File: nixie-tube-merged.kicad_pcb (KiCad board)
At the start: 2 copper layers, 99.8 x 97.5 mm, 0 parts

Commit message: finalized everything and ready to send out
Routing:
- net (no net): track 5710.5 -> 0.00 mm, vias 964 -> 0

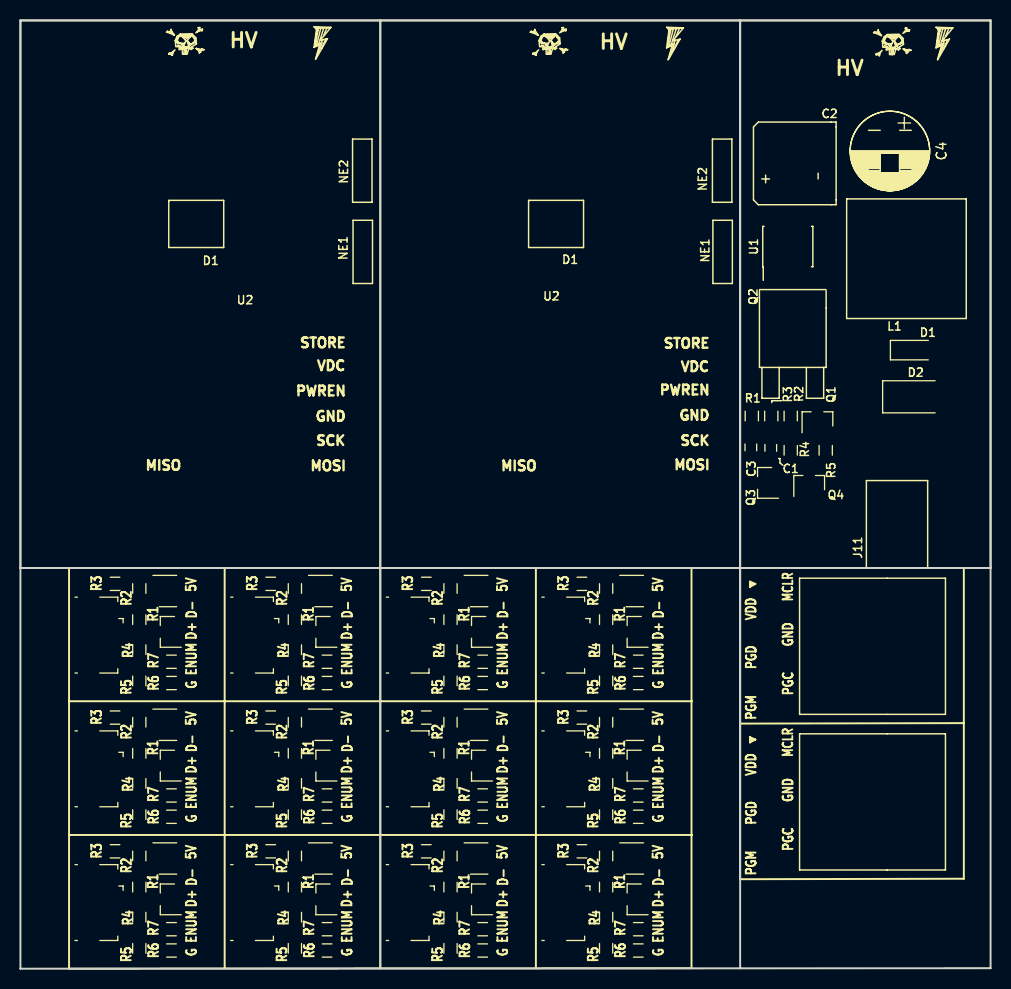
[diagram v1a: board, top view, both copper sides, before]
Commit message: added via stiching around the board
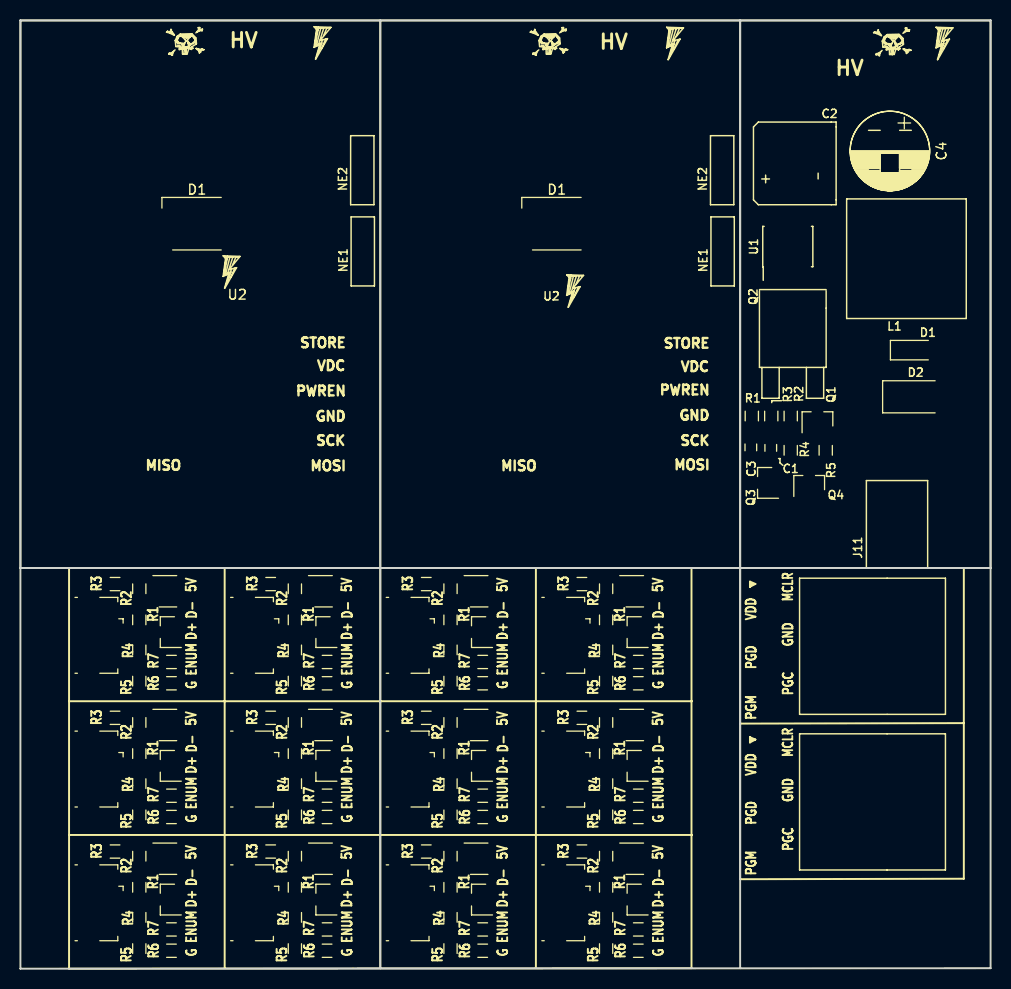
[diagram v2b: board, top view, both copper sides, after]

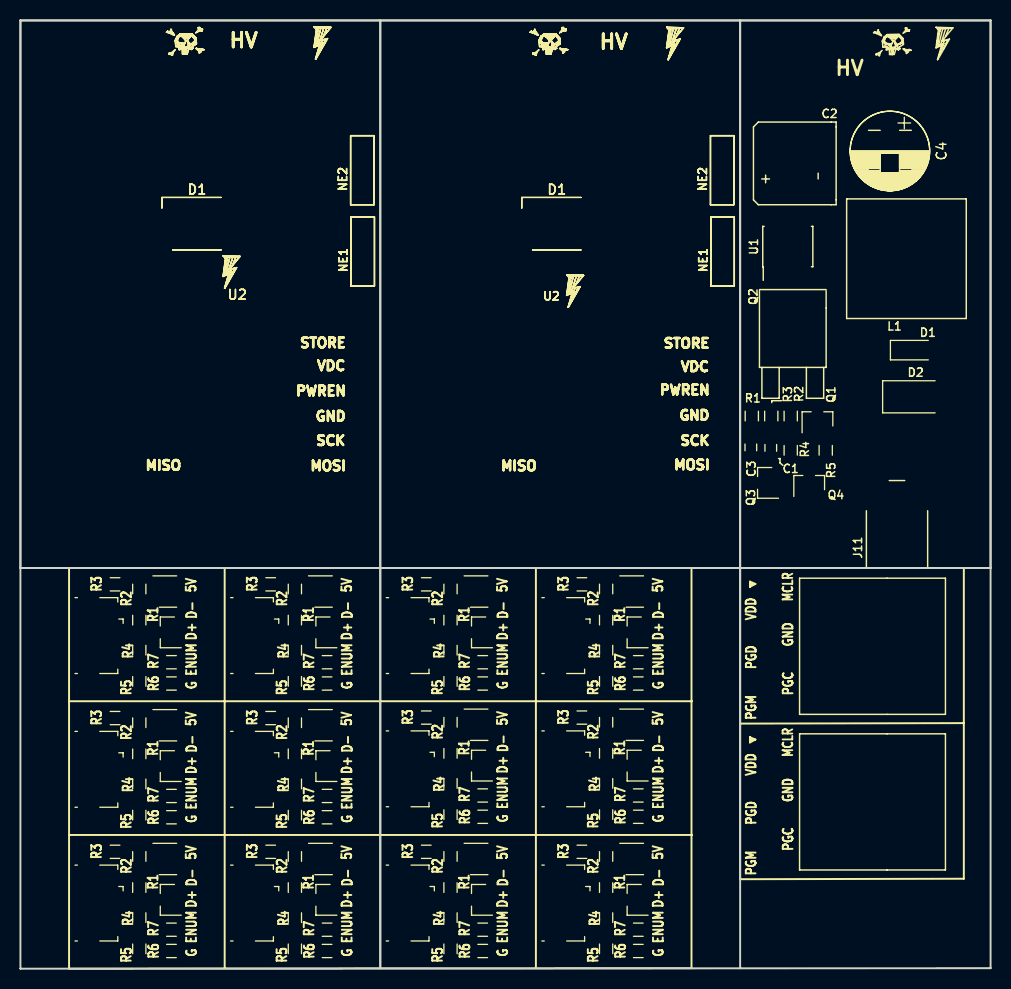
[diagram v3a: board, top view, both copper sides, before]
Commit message: added fire symbol at the back of the board
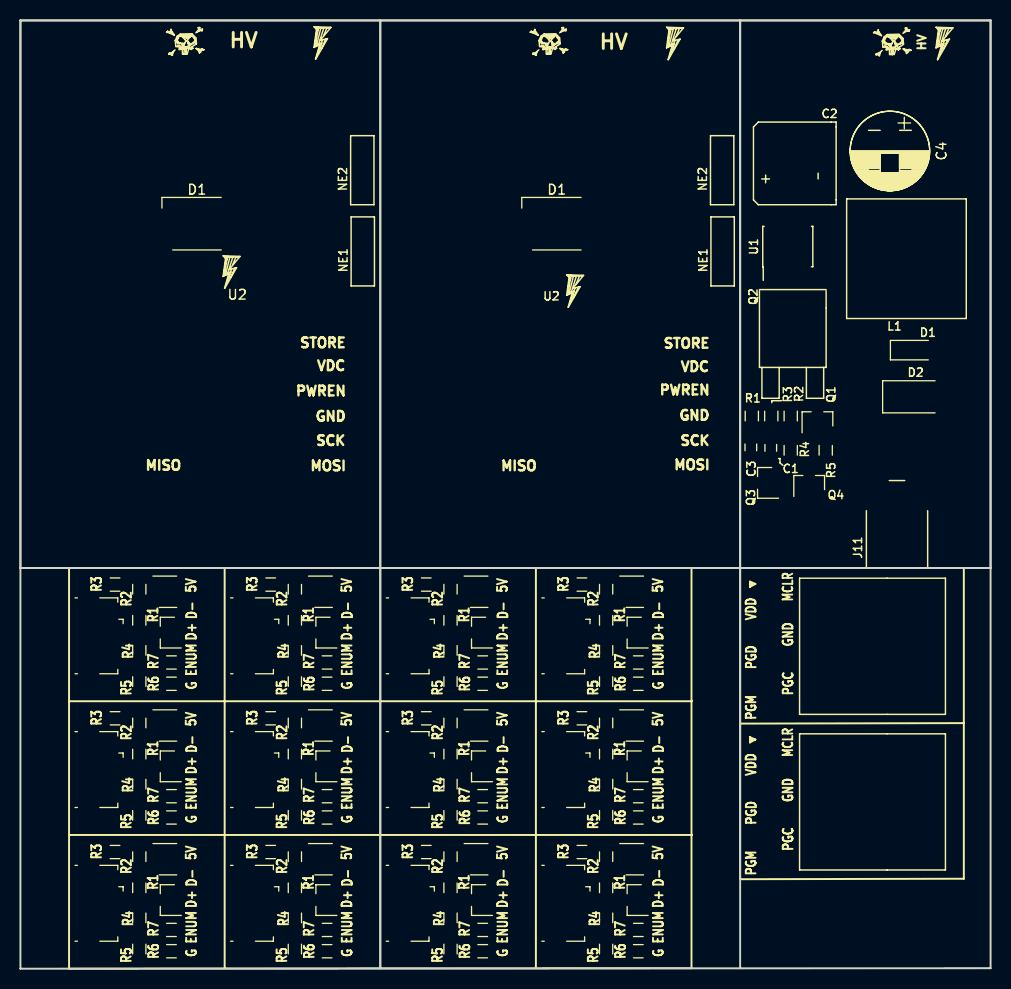
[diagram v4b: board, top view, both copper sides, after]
